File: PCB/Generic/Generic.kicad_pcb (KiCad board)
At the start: 2 copper layers, 30 x 30.2 mm, 29 parts, among them J1 DC, J2 USB-C, J3 Shelly, J4 Conn_01x05, Q1 CJ2301, U1 MD8942, U2 ESP32-PICO-MINI-02, U3 CH340X, U5 QR

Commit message: New caps
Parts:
- turned R7 to 0 degrees
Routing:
- net GND: track 37.4 -> 39.5 mm, vias 9 -> 11
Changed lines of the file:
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@@
   )
   (footprint "RevK:R_0402" (layer "B.Cu")
-    (at 101 143.2 180)
+    (at 101 143.2)
     (property "Sheetfile" "Generic.kicad_sch")
     (property "Sheetname" "")
@@
     (property "ki_keywords" "R res resistor")
     (attr smd)
-    (fp_text reference "R7" (at 0.4 0.9 unlocked) (layer "B.SilkS") hide
+    (fp_text reference "R7" (at 0.4 0.9 -180 unlocked) (layer "B.SilkS") hide
         (effects (font (size 1 1) (thickness 0.15)) (justify mirror))
     )
-    (fp_text value "40k2" (at 0 -1.1 unlocked) (layer "B.Fab") hide
+    (fp_text value "40k2" (at 0 -1.1 -180 unlocked) (layer "B.Fab") hide
         (effects (font (size 1 1) (thickness 0.15)) (justify mirror))
     )
-    (fp_text user "${VALUE}" (at 0 0 unlocked) (layer "B.Fab")
+    (fp_text user "${VALUE}" (at 0 0 -180 unlocked) (layer "B.Fab")
         (effects (font (size 0.3 0.3) (thickness 0.05)) (justify mirror))
     )
@@
     (fp_line (start 0.75 0.35) (end 0.75 -0.35)
       (stroke (width 0.05) (type solid)) (layer "Dwgs.User"))
-    (pad "1" smd roundrect (at -0.5 0 180) (size 0.54 0.64) (layers "B.Cu" "B.Paste" "B.Mask") (roundrect_rratio 0.25)
+    (pad "1" smd roundrect (at -0.5 0) (size 0.54 0.64) (layers "B.Cu" "B.Paste" "B.Mask") (roundrect_rratio 0.25)
       (net 2 "GND") (pintype "passive"))
-    (pad "2" smd roundrect (at 0.5 0 180) (size 0.54 0.64) (layers "B.Cu" "B.Paste" "B.Mask") (roundrect_rratio 0.25)
+    (pad "2" smd roundrect (at 0.5 0) (size 0.54 0.64) (layers "B.Cu" "B.Paste" "B.Mask") (roundrect_rratio 0.25)
       (net 24 "Net-(U1-FB)") (pintype "passive"))
     (model "${KICAD6_3DMODEL_DIR}/Resistor_SMD.3dshapes/R_0402_1005Metric.wrl"
@@
     (descr "Capacitor SMD 0603 (1608 Metric), square (rectangular) end terminal, IPC_7351 nominal, (Body size source: IPC-SM-782 page 76, https://www.pcb-3d.com/wordpress/wp-content/uploads/ipc-sm-782a_amendment_1_and_2.pdf), generated with kicad-footprint-generator")
     (tags "capacitor")
-    (property "LCSC Part #" "C1525")
+    (property "LCSC Part #" "C1691")
     (property "Sheetfile" "Generic.kicad_sch")
     (property "Sheetname" "")
@@
   (arc (start 106.071751 135.25) (mid 105.451134 135.126552) (end 104.925 134.775) (width 0.2) (layer "B.Cu") (net 1))
   (arc (start 107.53967 135.25) (mid 107.348985 135.328985) (end 107.27 135.51967) (width 0.2) (layer "B.Cu") (net 1))
+  (via (at 107 146.8) (size 0.8) (drill 0.4) (layers "F.Cu" "B.Cu") (free) (net 2))
   (via (at 96.070248 144.297605) (size 0.8) (drill 0.4) (layers "F.Cu" "B.Cu") (free) (net 2))
   (via (at 88.95 136.85) (size 0.8) (drill 0.4) (layers "F.Cu" "B.Cu") (free) (net 2))
+  (via (at 99.1 142.8) (size 0.8) (drill 0.4) (layers "F.Cu" "B.Cu") (free) (net 2))
   (via (at 87.9 142.6) (size 0.8) (drill 0.4) (layers "F.Cu" "B.Cu") (net 2))
   (via (at 88.2 148.5) (size 0.8) (drill 0.4) (layers "F.Cu" "B.Cu") (free) (net 2))
@@
   (segment (start 103.675 133.1) (end 102.8 133.1) (width 0.5) (layer "B.Cu") (net 2))
   (segment (start 108.075 139.24) (end 108.655 139.82) (width 0.25) (layer "B.Cu") (net 2))
+  (segment (start 100.5 145.025) (end 100.3 145.225) (width 0.25) (layer "B.Cu") (net 2))
   (segment (start 102.8 133.1) (end 101.8 133.1) (width 0.5) (layer "B.Cu") (net 2))
   (segment (start 97.75 130.85) (end 98.166712 130.433288) (width 0.25) (layer "B.Cu") (net 2))
@@
   (segment (start 101.6625 145.05) (end 100.722487 145.05) (width 0.6) (layer "B.Cu") (net 2))
   (segment (start 104.108637 130.987983) (end 104.25 131.129346) (width 0.25) (layer "B.Cu") (net 2))
+  (segment (start 100.5 143.2) (end 100.5 145.025) (width 0.25) (layer "B.Cu") (net 2))
   (segment (start 103.8 135.4) (end 104.325 135.4) (width 0.25) (layer "B.Cu") (net 2))
   (segment (start 98.760399 129) (end 98.760399 128.5454) (width 0.25) (layer "B.Cu") (net 2))
@@
   (segment (start 101.3 149.189213) (end 101.3 149.6) (width 1) (layer "B.Cu") (net 4))
   (segment (start 99.4 134.4) (end 98.575 134.4) (width 0.25) (layer "B.Cu") (net 4))
+  (segment (start 103.3 143.2) (end 103.270538 143.2) (width 0.25) (layer "B.Cu") (net 4))
   (segment (start 99.304862 131.932891) (end 99.304862 131.930976) (width 0.25) (layer "B.Cu") (net 4))
   (segment (start 99.4 135.9) (end 98.775 135.9) (width 0.25) (layer "B.Cu") (net 4))
   (segment (start 98.925 133.3) (end 98.925 132.709119) (width 0.25) (layer "B.Cu") (net 4))
   (segment (start 87.175 131.775) (end 87.75 131.775) (width 0.25) (layer "B.Cu") (net 4))
-  (segment (start 102.75 148.15) (end 102.75 144.1) (width 0.25) (layer "B.Cu") (net 4))
   (segment (start 86.853375 148.353375) (end 87.20864 147.998109) (width 0.25) (layer "B.Cu") (net 4))
   (segment (start 95.85 131.5) (end 94.9 131.5) (width 0.25) (layer "B.Cu") (net 4))
@@
   (segment (start 100.25 131.4) (end 99.835838 131.4) (width 0.25) (layer "B.Cu") (net 4))
   (segment (start 99.835838 131.4) (end 99.304862 131.930976) (width 0.25) (layer "B.Cu") (net 4))
-  (segment (start 103.270538 143.2) (end 103.018321 143.452217) (width 0.25) (layer "B.Cu") (net 4))
+  (segment (start 102.517157 148.382842) (end 102.2 148.7) (width 0.25) (layer "B.Cu") (net 4))
+  (segment (start 102.2 148.7) (end 101.3 149.6) (width 0.25) (layer "B.Cu") (net 4))
   (segment (start 99.053209 132.184544) (end 99.304862 131.932891) (width 0.25) (layer "B.Cu") (net 4))
   (segment (start 100.25 131.4) (end 102.15 131.4) (width 0.25) (layer "B.Cu") (net 4))
@@
   (segment (start 100.3 146.775) (end 99.425 146.775) (width 0.25) (layer "B.Cu") (net 4))
   (segment (start 98.575 134.4) (end 97.765685 134.4) (width 0.25) (layer "B.Cu") (net 4))
+  (segment (start 102.8 144.335979) (end 102.8 147.7) (width 0.25) (layer "B.Cu") (net 4))
   (segment (start 98.925 133.3) (end 100.525 133.3) (width 0.25) (layer "B.Cu") (net 4))
   (arc (start 94.9 131.5) (mid 94.546447 131.646447) (end 94.4 132) (width 0.25) (layer "B.Cu") (net 4))
   (arc (start 88.450498 145) (mid 88.12775 146.622565) (end 87.20864 147.998109) (width 0.25) (layer "B.Cu") (net 4))
   (arc (start 98.775 135.9) (mid 98.633579 135.841421) (end 98.575 135.7) (width 0.25) (layer "B.Cu") (net 4))
-  (arc (start 101.3 149.6) (mid 102.325305 149.175305) (end 102.75 148.15) (width 0.25) (layer "B.Cu") (net 4))
+  (arc (start 102.8 147.7) (mid 102.726492 148.069552) (end 102.517157 148.382842) (width 0.25) (layer "B.Cu") (net 4))
   (arc (start 97.765685 134.4) (mid 97.24306 134.296043) (end 96.8 134) (width 0.25) (layer "B.Cu") (net 4))
-  (arc (start 103.018321 143.452217) (mid 102.819734 143.749422) (end 102.75 144.1) (width 0.25) (layer "B.Cu") (net 4))
   (arc (start 86.000253 148.70675) (mid 86.461959 148.614911) (end 86.853375 148.353375) (width 0.25) (layer "B.Cu") (net 4))
   (arc (start 86.7 132.25) (mid 86.839124 131.914124) (end 87.175 131.775) (width 0.25) (layer "B.Cu") (net 4))
   (arc (start 88.5 135.1) (mid 87.227208 134.572792) (end 86.7 133.3) (width 0.25) (layer "B.Cu") (net 4))
+  (arc (start 103.270538 143.2) (mid 102.922289 143.721191) (end 102.8 144.335979) (width 0.25) (layer "B.Cu") (net 4))
   (arc (start 98.925 133.3) (mid 98.665962 133.687677) (end 98.575 134.144974) (width 0.25) (layer "B.Cu") (net 4))
   (arc (start 100.3 146.775) (mid 101.040108 147.88265) (end 101.3 149.189213) (width 1) (layer "B.Cu") (net 4))
@@
   (arc (start 86.95 140.938548) (mid 87.058184 140.39467) (end 87.366267 139.933591) (width 0.25) (layer "B.Cu") (net 23))
   (segment (start 102.3 143.2) (end 102.3 143.4625) (width 0.25) (layer "B.Cu") (net 24))
-  (segment (start 100.5 143.2) (end 101.4 144.1) (width 0.25) (layer "B.Cu") (net 24))
+  (segment (start 102.3 143.2) (end 101.5 143.2) (width 0.25) (layer "B.Cu") (net 24))
   (arc (start 102.3 143.4625) (mid 102.113281 143.913281) (end 101.6625 144.1) (width 0.25) (layer "B.Cu") (net 24))
   (segment (start 102.025 147) (end 102.025 146.3625) (width 0.25) (layer "B.Cu") (net 45))

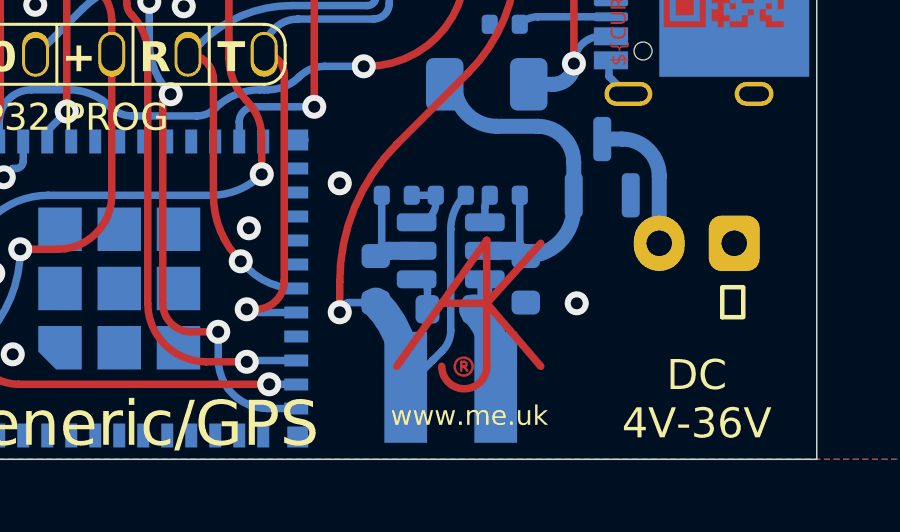
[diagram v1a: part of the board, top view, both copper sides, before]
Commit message: New regulator
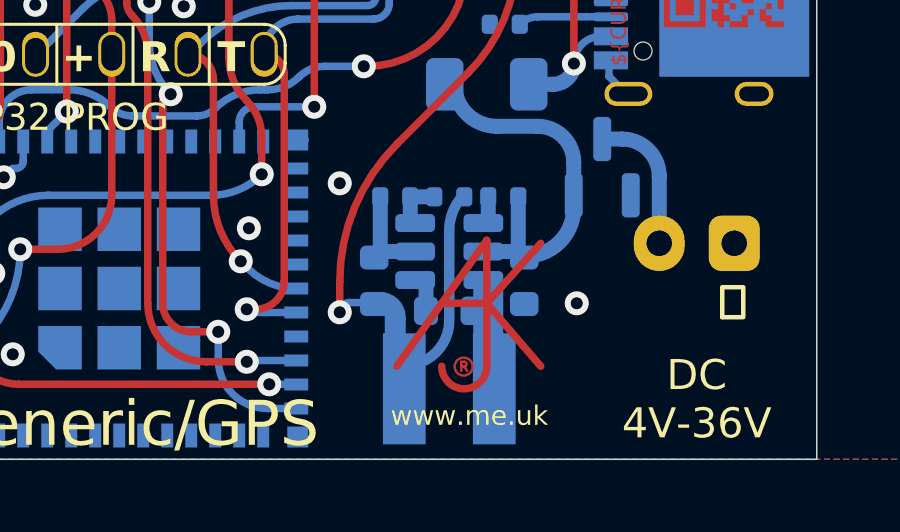
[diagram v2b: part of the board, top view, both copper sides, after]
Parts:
- removed C2: 10uF 50V, RevK:C_0603
- removed C3: 100nF, RevK:C_0603
- removed C4: 10uF 16V, RevK:C_0603
- removed L1: 10uH, RevK:L_4x4
- removed R4: 450k, RevK:R_0402
- removed R5: 124k, RevK:R_0402
- removed R7: 40k2, RevK:R_0402
- removed U1: MD8942, RevK:SOT-23-6
- added C5: 10uF 50V, RevK:C_0603_, B.Cu at (105.2, 146.1)
- added C6: 10uF 6.3V, RevK:C_0603_, B.Cu at (100.2, 146.1)
- added C7: 100nF, RevK:C_0603_, B.Cu at (102.8, 147.1)
- added L2: 10uH, RevK:L_4x4_, B.Cu at (102.8, 149.7)
- added R12: 40k2, RevK:R_0402_, B.Cu at (101.0, 143.2)
- added R13: 1M, RevK:R_0402_, B.Cu at (104.5, 143.2)
- added R8: 124k, RevK:R_0402_, B.Cu at (102.8, 143.2)
- added U4: MD8942, RevK:SOT-23-6-MD8942, B.Cu at (102.8, 145.1)
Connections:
- net VBUS renamed Net-(D1-A)
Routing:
- net +3.3V: track 90.0 -> 79.8 mm
- net DC: track 13.7 -> 9.32 mm
- net Net-(U1-SW): track 3.97 -> 0.00 mm
- net GND: track 39.5 -> 36.0 mm
- net Net-(U1-FB): track 2.04 -> 0.00 mm
- net Net-(U1-BST): track 1.19 -> 0.00 mm
- net Net-(U1-EN): track 0.94 -> 0.00 mm

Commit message: Tidy regulator
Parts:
- moved U4 0.31 mm to (103.0, 144.9)
- moved C5 0.29 mm to (105.5, 145.9)
- moved C6 0.29 mm to (100.5, 145.9)
- moved C7 0.29 mm to (103.0, 146.9)
- moved L2 0.29 mm to (103.0, 149.5)
- moved R12 0.29 mm to (101.2, 143.1)
- moved R13 0.29 mm to (104.8, 143.1)
- moved R8 0.27 mm to (103.0, 143.1)
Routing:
- net +3.3V: track 79.8 -> 78.8 mm

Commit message: Tweak
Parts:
- moved R10 0.57 mm to (89.1, 133.1)
- moved R11 0.57 mm to (89.1, 131.3)
- moved R9 0.57 mm to (89.1, 132.2)
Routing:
- net GND: track 36.0 -> 38.8 mm
- net Net-(D1-A): track 12.0 -> 12.7 mm
- net Net-(D2-RK): track 1.36 -> 0.79 mm
- net Net-(D2-BK): track 1.48 -> 0.98 mm

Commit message: Tidy reg
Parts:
- moved R12 1.12 mm to (100.7, 144.1), turned to 90 degrees
- moved R13 1.12 mm to (105.3, 144.1), turned to -90 degrees
- moved C5 0.30 mm to (105.5, 146.2)
- moved C6 0.30 mm to (100.5, 146.2)
- moved R8 0.10 mm to (103.0, 143.0), turned to 180 degrees

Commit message: SIlk
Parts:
- moved C7 0.20 mm to (103.0, 146.7)
- moved U4 0.20 mm to (103.0, 144.7)
- moved C5 0.20 mm to (105.5, 146.0)
- moved C6 0.20 mm to (100.5, 146.0)
- moved L2 0.20 mm to (103.0, 149.3)
- moved R12 0.20 mm to (100.7, 143.9)
- moved R13 0.20 mm to (105.3, 143.9)
- moved R8 0.20 mm to (103.0, 142.8)
